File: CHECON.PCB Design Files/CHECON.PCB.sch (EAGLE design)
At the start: 71 parts, among them T1 BC849, U2 MAX232SOIC16, U3 RS485SOIC, X1 53047-02

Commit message: sync repo
Sync work while rafael was out
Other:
- moved on the sheet: U$49
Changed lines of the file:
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@@
 <grid distance="0.1" unitdist="inch" unit="inch" style="lines" multiple="1" display="no" altdistance="0.01" altunitdist="inch" altunit="inch"/>
 <layers>
-<layer number="1" name="Top" color="4" fill="1" visible="yes" active="no"/>
-<layer number="2" name="GRB2" color="1" fill="3" visible="yes" active="no"/>
-<layer number="3" name="Route3" color="4" fill="3" visible="yes" active="no"/>
-<layer number="4" name="Route4" color="1" fill="4" visible="yes" active="no"/>
-<layer number="5" name="Route5" color="4" fill="4" visible="yes" active="no"/>
-<layer number="6" name="Route6" color="1" fill="8" visible="yes" active="no"/>
-<layer number="7" name="Route7" color="4" fill="8" visible="yes" active="no"/>
-<layer number="8" name="Route8" color="1" fill="2" visible="yes" active="no"/>
-<layer number="9" name="Route9" color="4" fill="2" visible="yes" active="no"/>
-<layer number="10" name="Route10" color="1" fill="7" visible="yes" active="no"/>
-<layer number="11" name="Route11" color="4" fill="7" visible="yes" active="no"/>
-<layer number="12" name="Route12" color="1" fill="5" visible="yes" active="no"/>
-<layer number="13" name="Route13" color="4" fill="5" visible="yes" active="no"/>
-<layer number="14" name="Route14" color="1" fill="6" visible="yes" active="no"/>
-<layer number="15" name="Route15" color="4" fill="6" visible="yes" active="no"/>
-<layer number="16" name="Bottom" color="1" fill="1" visible="yes" active="no"/>
-<layer number="17" name="Pads" color="2" fill="1" visible="yes" active="no"/>
-<layer number="18" name="Vias" color="2" fill="1" visible="yes" active="no"/>
-<layer number="19" name="Unrouted" color="6" fill="1" visible="yes" active="no"/>
-<layer number="20" name="Dimension" color="15" fill="1" visible="yes" active="no"/>
-<layer number="21" name="tPlace" color="7" fill="1" visible="yes" active="no"/>
-<layer number="22" name="bPlace" color="7" fill="1" visible="yes" active="no"/>
-<layer number="23" name="tOrigins" color="15" fill="1" visible="yes" active="no"/>
-<layer number="24" name="bOrigins" color="15" fill="1" visible="yes" active="no"/>
-<layer number="25" name="tNames" color="7" fill="1" visible="yes" active="no"/>
-<layer number="26" name="bNames" color="7" fill="1" visible="yes" active="no"/>
-<layer number="27" name="tValues" color="7" fill="1" visible="yes" active="no"/>
-<layer number="28" name="bValues" color="7" fill="1" visible="yes" active="no"/>
+<layer number="1" name="Top" color="4" fill="1" visible="no" active="no"/>
+<layer number="2" name="GRB2" color="1" fill="3" visible="no" active="no"/>
+<layer number="3" name="Route3" color="4" fill="3" visible="no" active="no"/>
+<layer number="4" name="Route4" color="1" fill="4" visible="no" active="no"/>
+<layer number="5" name="Route5" color="4" fill="4" visible="no" active="no"/>
+<layer number="6" name="Route6" color="1" fill="8" visible="no" active="no"/>
+<layer number="7" name="Route7" color="4" fill="8" visible="no" active="no"/>
+<layer number="8" name="Route8" color="1" fill="2" visible="no" active="no"/>
+<layer number="9" name="Route9" color="4" fill="2" visible="no" active="no"/>
+<layer number="10" name="Route10" color="1" fill="7" visible="no" active="no"/>
+<layer number="11" name="Route11" color="4" fill="7" visible="no" active="no"/>
+<layer number="12" name="Route12" color="1" fill="5" visible="no" active="no"/>
+<layer number="13" name="Route13" color="4" fill="5" visible="no" active="no"/>
+<layer number="14" name="Route14" color="1" fill="6" visible="no" active="no"/>
+<layer number="15" name="Route15" color="4" fill="6" visible="no" active="no"/>
+<layer number="16" name="Bottom" color="1" fill="1" visible="no" active="no"/>
+<layer number="17" name="Pads" color="2" fill="1" visible="no" active="no"/>
+<layer number="18" name="Vias" color="2" fill="1" visible="no" active="no"/>
+<layer number="19" name="Unrouted" color="6" fill="1" visible="no" active="no"/>
+<layer number="20" name="Dimension" color="15" fill="1" visible="no" active="no"/>
+<layer number="21" name="tPlace" color="7" fill="1" visible="no" active="no"/>
+<layer number="22" name="bPlace" color="7" fill="1" visible="no" active="no"/>
+<layer number="23" name="tOrigins" color="15" fill="1" visible="no" active="no"/>
+<layer number="24" name="bOrigins" color="15" fill="1" visible="no" active="no"/>
+<layer number="25" name="tNames" color="7" fill="1" visible="no" active="no"/>
+<layer number="26" name="bNames" color="7" fill="1" visible="no" active="no"/>
+<layer number="27" name="tValues" color="7" fill="1" visible="no" active="no"/>
+<layer number="28" name="bValues" color="7" fill="1" visible="no" active="no"/>
 <layer number="29" name="tStop" color="7" fill="3" visible="no" active="no"/>
 <layer number="30" name="bStop" color="7" fill="6" visible="no" active="no"/>
@@
 <layer number="35" name="tGlue" color="7" fill="4" visible="no" active="no"/>
 <layer number="36" name="bGlue" color="7" fill="5" visible="no" active="no"/>
-<layer number="37" name="tTest" color="7" fill="1" visible="yes" active="no"/>
-<layer number="38" name="bTest" color="7" fill="1" visible="yes" active="no"/>
+<layer number="37" name="tTest" color="7" fill="1" visible="no" active="no"/>
+<layer number="38" name="bTest" color="7" fill="1" visible="no" active="no"/>
 <layer number="39" name="tKeepout" color="4" fill="11" visible="no" active="no"/>
 <layer number="40" name="bKeepout" color="1" fill="11" visible="no" active="no"/>
@@
 <layer number="44" name="Drills" color="7" fill="1" visible="no" active="no"/>
 <layer number="45" name="Holes" color="7" fill="1" visible="no" active="no"/>
-<layer number="46" name="Milling" color="3" fill="1" visible="yes" active="no"/>
-<layer number="47" name="Measures" color="7" fill="1" visible="yes" active="no"/>
-<layer number="48" name="Document" color="7" fill="1" visible="yes" active="no"/>
-<layer number="49" name="Reference" color="7" fill="1" visible="yes" active="no"/>
-<layer number="50" name="dxf" color="7" fill="1" visible="yes" active="no"/>
-<layer number="51" name="tDocu" color="7" fill="1" visible="yes" active="no"/>
-<layer number="52" name="bDocu" color="7" fill="1" visible="yes" active="no"/>
-<layer number="53" name="tGND_GNDA" color="7" fill="1" visible="yes" active="no"/>
-<layer number="54" name="bGND_GNDA" color="7" fill="1" visible="yes" active="no"/>
-<layer number="56" name="wert" color="7" fill="1" visible="yes" active="no"/>
-<layer number="57" name="tCAD" color="7" fill="1" visible="yes" active="no"/>
+<layer number="46" name="Milling" color="3" fill="1" visible="no" active="no"/>
+<layer number="47" name="Measures" color="7" fill="1" visible="no" active="no"/>
+<layer number="48" name="Document" color="7" fill="1" visible="no" active="no"/>
+<layer number="49" name="Reference" color="7" fill="1" visible="no" active="no"/>
+<layer number="50" name="dxf" color="7" fill="1" visible="no" active="no"/>
+<layer number="51" name="tDocu" color="7" fill="1" visible="no" active="no"/>
+<layer number="52" name="bDocu" color="7" fill="1" visible="no" active="no"/>
+<layer number="53" name="tGND_GNDA" color="7" fill="1" visible="no" active="no"/>
+<layer number="54" name="bGND_GNDA" color="7" fill="1" visible="no" active="no"/>
+<layer number="56" name="wert" color="7" fill="1" visible="no" active="no"/>
+<layer number="57" name="tCAD" color="7" fill="1" visible="no" active="no"/>
 <layer number="91" name="Nets" color="2" fill="1" visible="yes" active="yes"/>
 <layer number="92" name="Busses" color="1" fill="1" visible="yes" active="yes"/>
@@
 <attribute name="MFGN" x="88.9" y="78.74" size="1.778" layer="96" rot="R180" display="off"/>
 </instance>
-<instance part="U$49" gate="&gt;NAME" x="43.18" y="68.58" rot="R270">
-<attribute name="MFGP" x="43.18" y="68.58" size="1.778" layer="96" rot="R270" display="off"/>
-<attribute name="MFGN" x="43.18" y="68.58" size="1.778" layer="96" rot="R270" display="off"/>
-</instance>
-<instance part="+3V6" gate="G$1" x="43.18" y="76.2"/>
+<instance part="U$49" gate="&gt;NAME" x="45.72" y="68.58" rot="R270">
+<attribute name="MFGP" x="45.72" y="68.58" size="1.778" layer="96" rot="R270" display="off"/>
+<attribute name="MFGN" x="45.72" y="68.58" size="1.778" layer="96" rot="R270" display="off"/>
+</instance>
+<instance part="+3V6" gate="G$1" x="45.72" y="78.74"/>
 <instance part="U$50" gate="G$1" x="-33.02" y="93.98"/>
 <instance part="U$51" gate="G$1" x="-33.02" y="86.36"/>
@@
 <pinref part="U$49" gate="&gt;NAME" pin="1"/>
 <pinref part="+3V6" gate="G$1" pin="+3V3"/>
+<wire x1="45.72" y1="76.2" x2="45.72" y2="73.66" width="0.1524" layer="91"/>
 </segment>
 <segment>
@@
 <pinref part="U$3" gate="G$1" pin="RST"/>
 <pinref part="U$49" gate="&gt;NAME" pin="2"/>
-<wire x1="33.02" y1="58.42" x2="43.18" y2="58.42" width="0.1524" layer="91"/>
-<wire x1="43.18" y1="58.42" x2="43.18" y2="63.5" width="0.1524" layer="91"/>
+<wire x1="33.02" y1="58.42" x2="45.72" y2="58.42" width="0.1524" layer="91"/>
+<wire x1="45.72" y1="58.42" x2="45.72" y2="63.5" width="0.1524" layer="91"/>
 <pinref part="JP2" gate="A" pin="10"/>
-<wire x1="71.12" y1="63.5" x2="43.18" y2="63.5" width="0.1524" layer="91"/>
-<junction x="43.18" y="63.5"/>
-</segment>
-</net>
+<wire x1="71.12" y1="63.5" x2="45.72" y2="63.5" width="0.1524" layer="91"/>
+<junction x="45.72" y="63.5"/>
+</segment>
+</net>

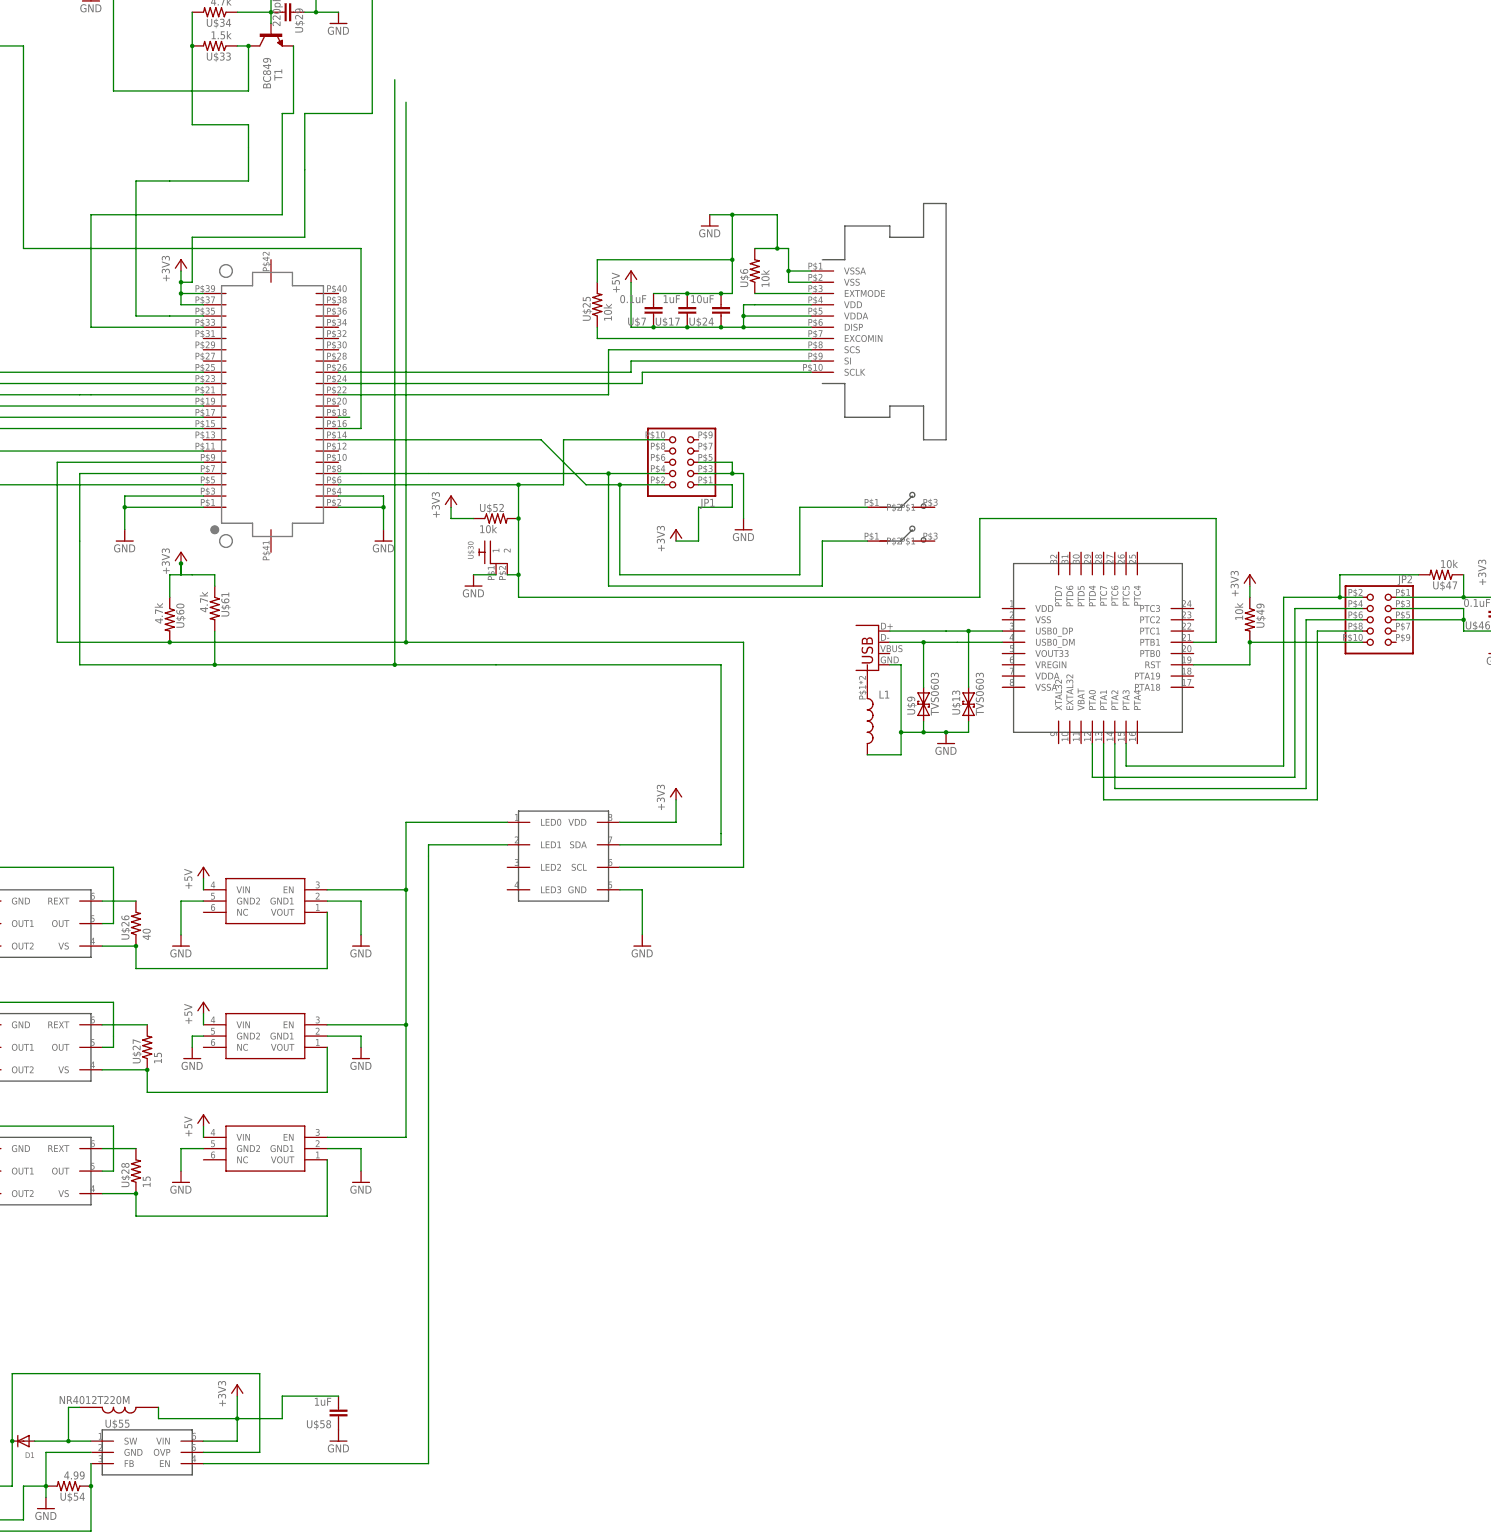
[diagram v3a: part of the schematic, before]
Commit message: Minor changes
Renamed some nets and worked on SWD section
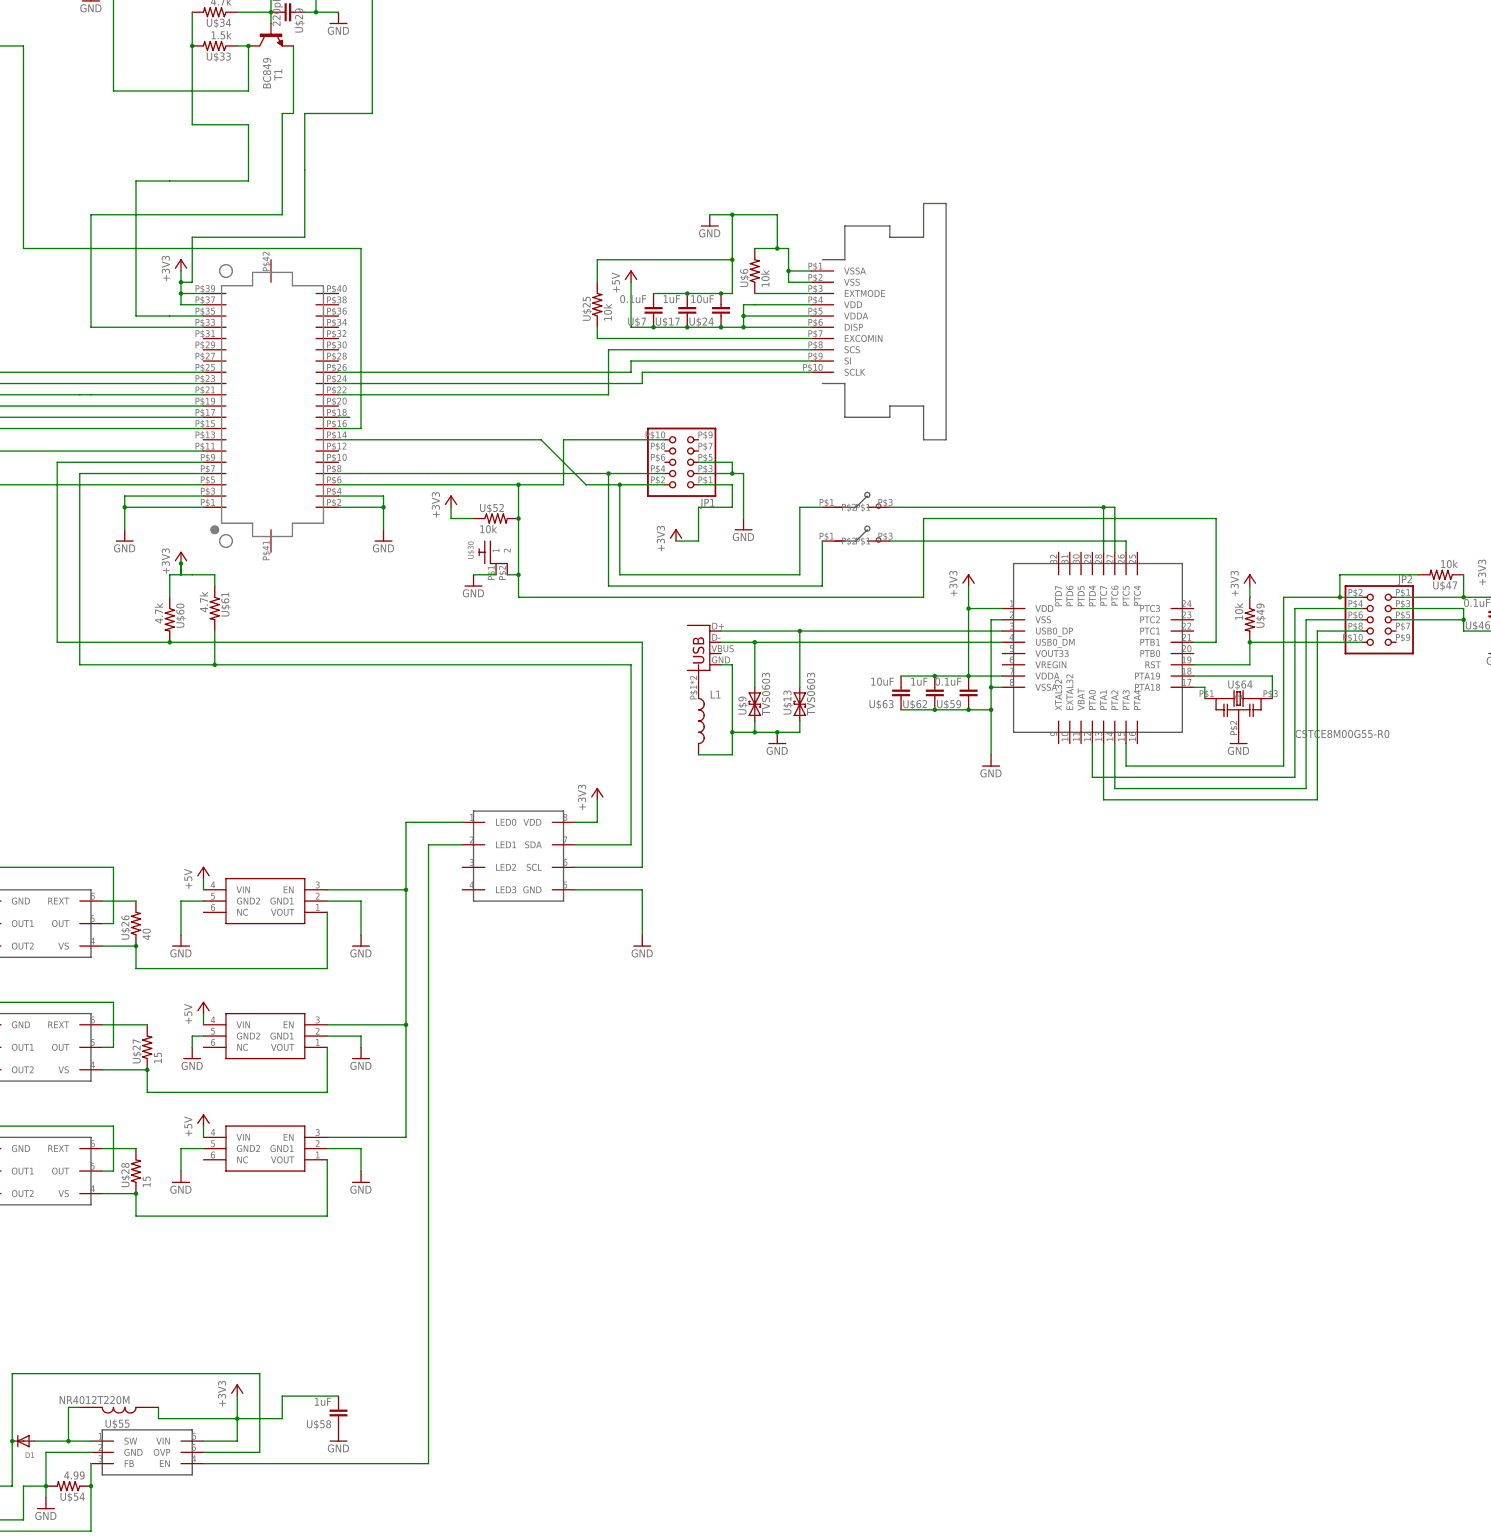
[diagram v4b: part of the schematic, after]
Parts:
- added U$59: 0.1uF, GW-devices:RF-C0805
- added U$62: 1uF, GW-devices:RF-C0805
- added U$63: 10uF, GW-devices:RF-C0805
- added U$64: CSTCE8M00G55-R0, KW2:CSTCE8M00G55-R0
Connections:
- net N$1 renamed SWD_DIO
- net N$4 renamed SWD_CLK
- net N$6 renamed RST
- new net N$1: U$3.PTC6, U$3.PTC7, U$50.P$2
- new net N$4: U$3.PTA18, U$64.1
- new net N$6: U$3.PTA19, U$64.3
- new net SWD_TGT_CLK: U$3.PTC5, U$51.P$2
- net +3V3: now also U$3.VDD, U$3.VDDA, U$59.2, U$62.2, U$63.2
- net GND: now also U$3.VSS, U$3.VSSA, U$59.1, U$62.1, U$63.1, U$64.2
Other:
- moved on the sheet: L1, U$13, U$9

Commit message: Working on layout
Layout
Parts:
- removed POSCON, SCANNER: RJ45-8, GW-devices:RJ45-8
- removed U$4: MIC94061C6, GW-devices:MIC94061C6
- removed U$48: 120, GW-devices:RF-R0805
- removed U$55: NR4012T220M, KW2:NR4012T220M
- added L2: (no value), SparkFun:INDUCTOR0603
- added P1, P2: RJ45-8PEGMOUNT, GW-devices:RJ45-8PEGMOUNT
- added R16, R17: 10k, GW-devices:RF-R0805
- added R2: 120, GW-devices:RF-R0805
- added SW1: CJS, KW2:CJS
- added U4: RS485SOIC, SparkFun:RS485SOIC
- L1: value (none) -> NR4012T220M; device SparkFun:INDUCTOR0603 -> KW2:NR4012T220M; MFGN TDK -> Taiyo Yuden; MFGP MPZ1608S331ATA00 -> NR4012T220M
- U3: value RS485SOIC -> MIC94061C6; device SparkFun:RS485SOIC -> GW-devices:MIC94061C6; PRICE 4.29 -> (none)
- renumbered U$1 to J1, U$10 to U10, U$11 to C1, U$12 to C2, U$13 to D4, U$14 to J2, U$15 to U8, U$16 to U9, U$17 to C12, U$18 to X2, U$19 to X3, U$2 to J3, U$20 to X4, U$21 to C3, U$22 to C4, U$23 to C5, U$24 to C13, U$25 to R14, U$26 to R5, U$27 to R7, U$28 to R6, U$29 to C7, U$3 to U12, U$30 to S1, U$31 to C10, U$32 to C9, U$33 to R10, U$34 to R9, U$35 to R12, U$36 to R3, U$37 to R1, U$38 to F2, U$39 to F4, U$40 to F6, U$41 to F1, U$42 to F3, U$43 to F5, U$44 to D2, U$45 to U11, U$46 to C17, U$47 to R19, U$49 to R18, U$5 to U5, U$50 to SW2, U$51 to SW3, U$52 to R13, U$53 to U6, U$54 to R4, U$56 to C6, U$57 to U1, U$58 to C8, U$59 to C16, U$6 to R15, U$60 to R8, U$61 to R11, U$62 to C15, U$63 to C14, U$64 to X5, U$7 to C11, U$8 to U7, U$9 to D3
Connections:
- removed net N$8: U8.EN
- new net N$24: R16.2, U12.USB0_DP
- new net N$59: R2.2, SW1.2
- new net N$60: R17.2, U12.USB0_DM
- net +3V3: now also L1.2; no longer U$55.2
- net GND: now also L2.2, P1.2, P2.2, P2.7, U3.GND1, U3.GND2, U4.GND; no longer L1.2, POSCON.2, POSCON.7, SCANNER.2, U$4.GND1, U$4.GND2, U3.GND
- net N$1: now also SW2.2; no longer SW2.P$2
- net N$12: now also P1.4; no longer SCANNER.4
- net N$17: now also U4.RO; no longer U3.RO
- net N$19: now also P2.4, R2.1, U4.B; no longer POSCON.4, U$48.1, U3.B
- net N$20: now also P2.5, SW1.1, U4.A; no longer POSCON.5, U$48.2, U3.A
- net N$25: now also P1.1, U3.VOUT; no longer SCANNER.1, U$4.VOUT
- net N$27: now also U4.DI; no longer U3.DI
- net N$28: now also U4./RE, U4.DE; no longer U3./RE, U3.DE
- net N$34: now also P1.5; no longer SCANNER.5
- net N$35: now also R17.1; no longer U12.USB0_DM
- net N$36: now also R16.1; no longer U12.USB0_DP
- net N$40: now also U3.EN; no longer U$4.EN
- net N$44: now also U8.EN
- net N$5: now also L2.1; no longer L1.1
- net N$50: now also L1.1; no longer U$55.1
- net N$7: now also P1.6; no longer SCANNER.6
- net R1IN: now also P1.3; no longer SCANNER.3
- net SWD_CLK: now also SW3.1; no longer SW3.P$1
- net SWD_DIO: now also SW2.1; no longer SW2.P$1
- net SWD_TGT_CLK: now also SW3.2; no longer SW3.P$2
- net V+: now also P2.1, P2.8, U3.VIN, U4.VCC; no longer POSCON.1, POSCON.8, U$4.VIN, U3.VCC
